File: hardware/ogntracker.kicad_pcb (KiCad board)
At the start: 2 copper layers, 50 x 84 mm, 29 parts, among them J1 ANT, J2 LX, J3 IGC, U1 STM32DEVBOARD, U2 RFM69HW, U3 VK2828U7G5LF, U4 MAX232

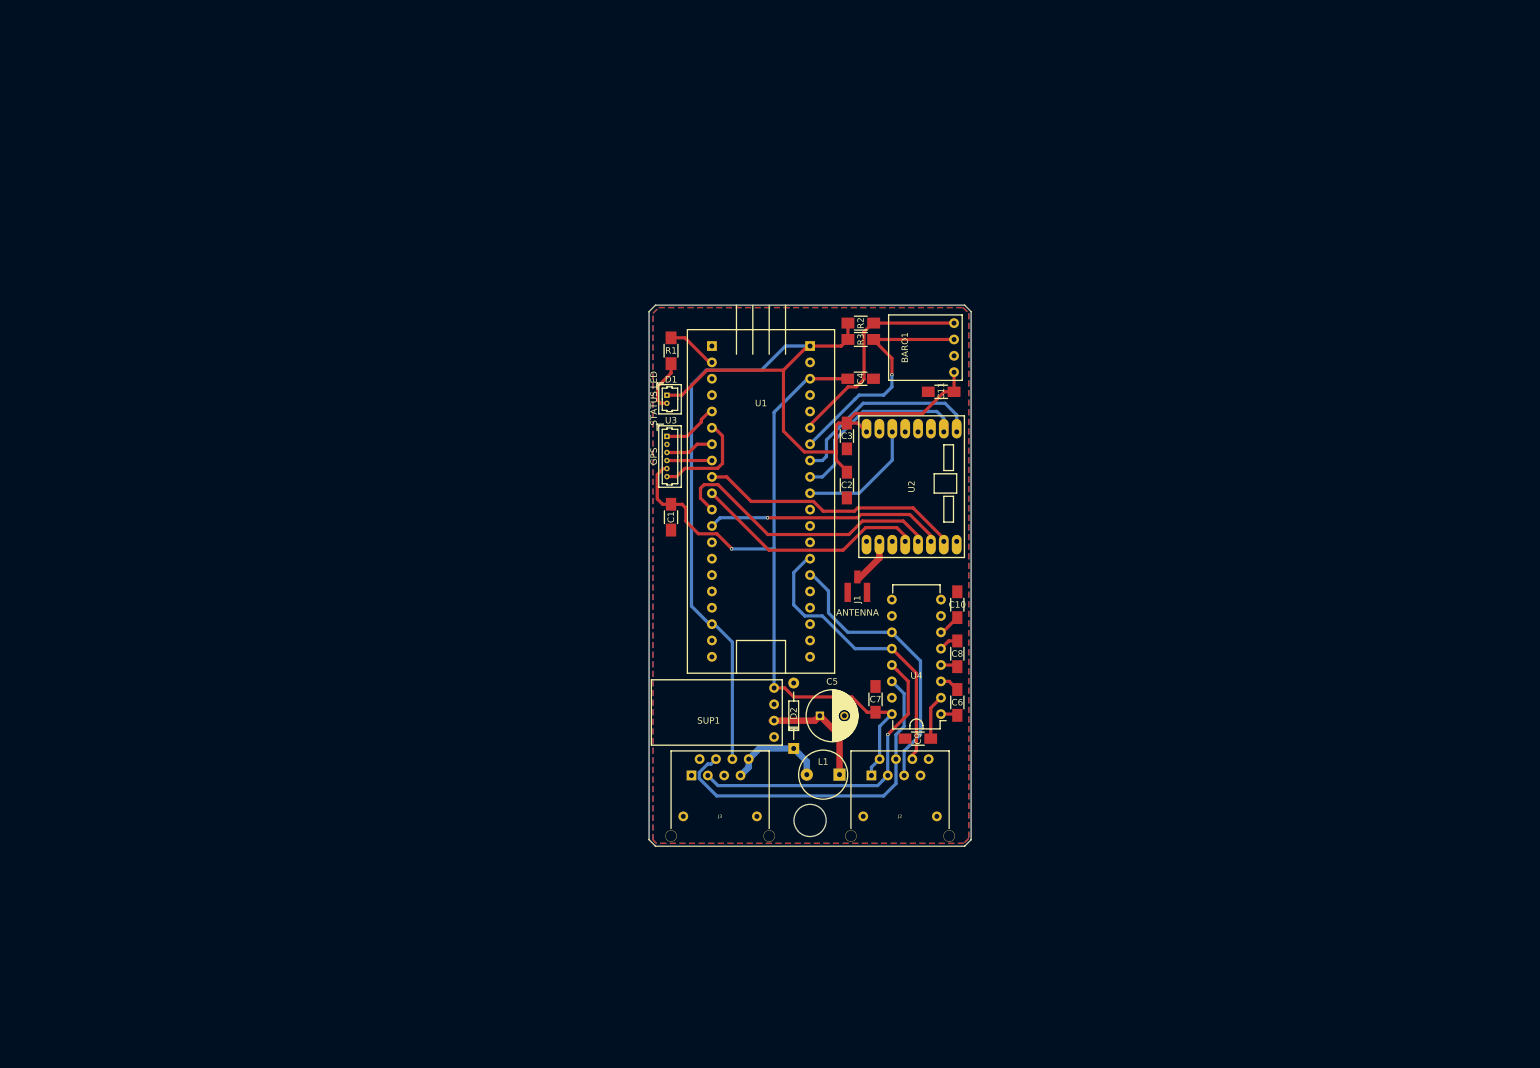
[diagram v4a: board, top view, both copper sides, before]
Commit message: Various updates to schematics and experiments with layout for new box
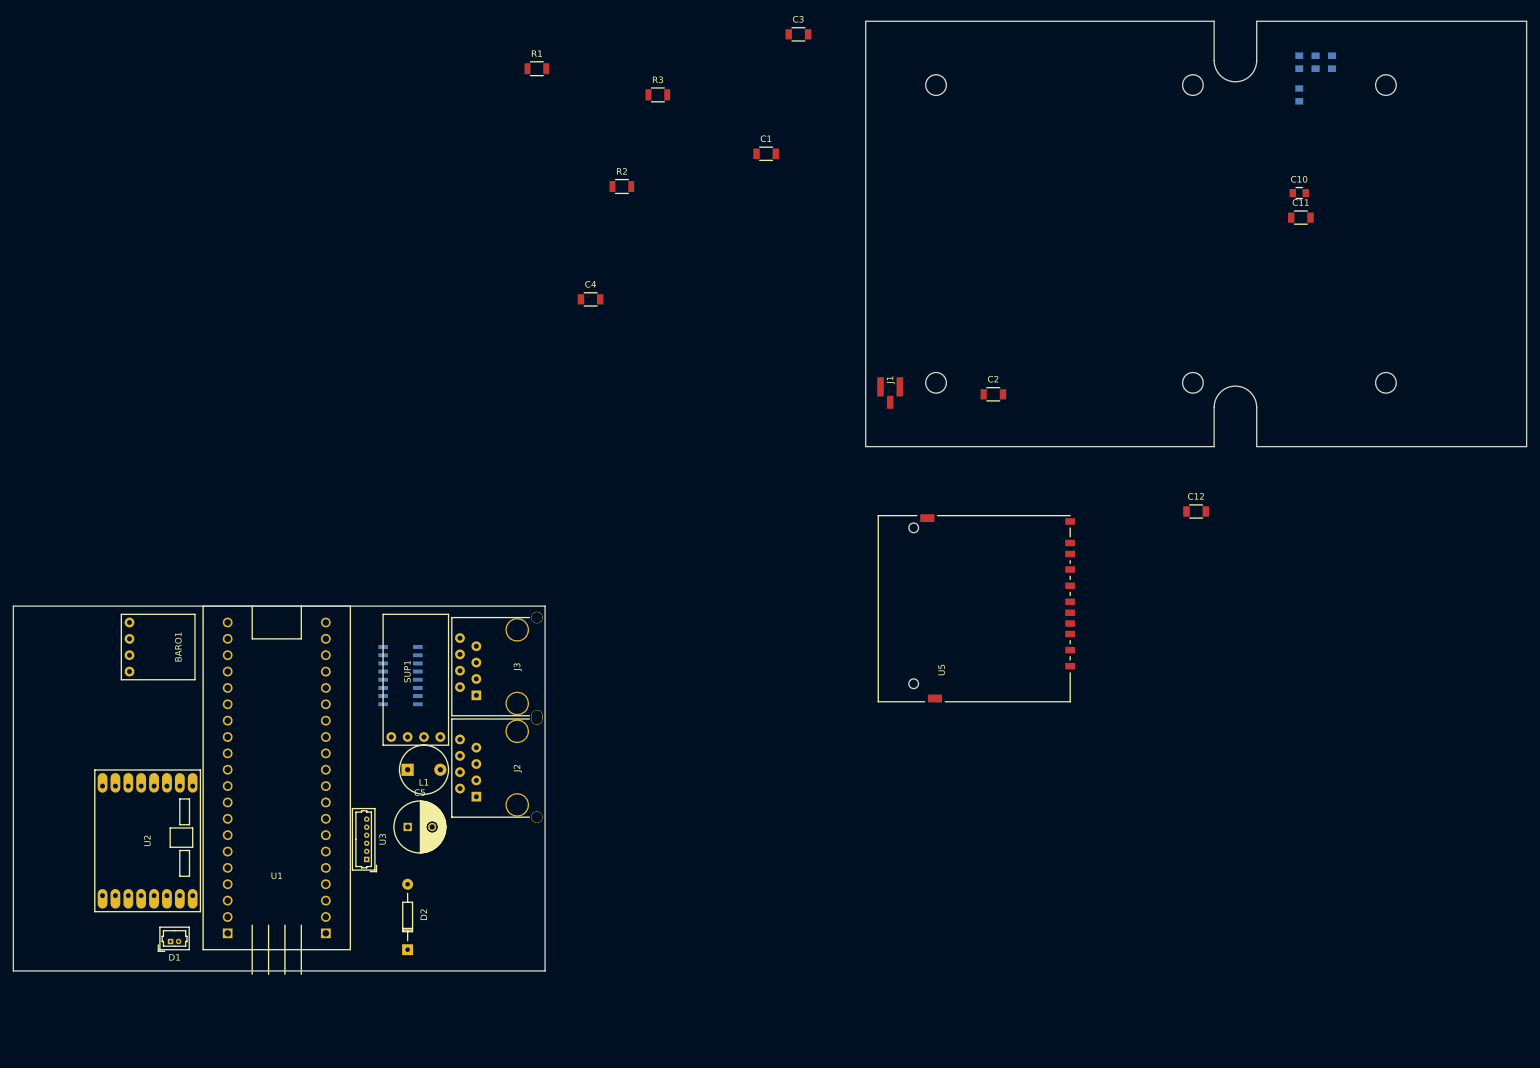
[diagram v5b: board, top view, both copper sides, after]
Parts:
- removed the REF** at (155.7, 152.7)
- removed REF***: OSHW-Logo2_7.3x6mm_SilkScreen, Symbols:OSHW-Logo2_7.3x6mm_SilkScreen
- removed REF***: KiCad-Logo2_6mm_SilkScreen, Symbols:KiCad-Logo2_6mm_SilkScreen
- added C12: 100nF, Capacitors_SMD:C_1206, F.Cu at (215.6, 104.7)
- added REF**: MountingHole_3.2mm_M3, Mounting_Holes:MountingHole_3.2mm_M3, F.Cu at (175.2, 84.8)
- added REF**: MountingHole_3.2mm_M3, Mounting_Holes:MountingHole_3.2mm_M3, F.Cu at (175.2, 38.5)
- added REF**: MountingHole_3.2mm_M3, Mounting_Holes:MountingHole_3.2mm_M3, F.Cu at (215.1, 84.8)
- added REF**: MountingHole_3.2mm_M3, Mounting_Holes:MountingHole_3.2mm_M3, F.Cu at (215.1, 38.5)
- added REF**: MountingHole_3.2mm_M3, Mounting_Holes:MountingHole_3.2mm_M3, F.Cu at (245.1, 38.5)
- added REF**: MountingHole_3.2mm_M3, Mounting_Holes:MountingHole_3.2mm_M3, F.Cu at (245.1, 84.8)
- added U5: SDCARD_SPI, Connect:SD_Card_Receptacle, F.Cu at (196.1, 119.4)
- C1, C11, C2, C3, C4: footprint Capacitors_SMD:C_1206_HandSoldering -> Capacitors_SMD:C_1206
- C10: footprint Capacitors_SMD:C_1206_HandSoldering -> Capacitors_SMD:C_0805
- C6, C7, C8, C9: footprint Capacitors_SMD:C_1206_HandSoldering -> Capacitors_SMD:C_0805; moved to B.Cu
- R1: value 330 -> 90; footprint Resistors_SMD:R_1206_HandSoldering -> Resistors_SMD:R_1206
- R2, R3: footprint Resistors_SMD:R_1206_HandSoldering -> Resistors_SMD:R_1206
- U4: footprint OGN Tracker:DIP-16_W7.62mm -> Housings_SOIC:SOIC-16_3.9x9.9mm_Pitch1.27mm; moved to B.Cu
- moved BARO1 131.4 mm to (52.6, 125.8), turned to 270 degrees
- moved U2 130.7 mm to (52.8, 155.9)
- moved C9 121.8 mm to (234.2, 35.0), turned to 270 degrees
- moved C7 121.7 mm to (236.7, 35.0)
- moved D1 114.6 mm to (56.4, 171.5), turned to 0 degrees
- moved C6 112.7 mm to (231.6, 35.0), turned to 270 degrees
- moved C8 101.7 mm to (231.6, 40.1), turned to 270 degrees
- moved U1 87.9 mm to (72.9, 147.4), turned to 180 degrees
- moved U4 84.1 mm to (92.1, 130.2), turned to 0 degrees
- moved C10 83.1 mm to (231.6, 55.3), turned to 0 degrees
- moved U3 80.5 mm to (86.9, 158.8), turned to 90 degrees
- moved D2 67.6 mm to (93.2, 172.8)
- moved C5 66.3 mm to (93.2, 153.7)
- moved C3 62.8 mm to (153.9, 30.7), turned to 0 degrees
- moved C11 62.1 mm to (231.9, 59.1), turned to 0 degrees
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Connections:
- U1 pad 37: (no net) -> /SD_MOSI
- U1 pad 38: (no net) -> /SD_MISO
- U1 pad 39: (no net) -> /SD_SCK
- U1 pad 40: (no net) -> /SD_CS
- U3 pad 1: /GPS_ENABLE -> /GPS_PPS
- U3 pad 2: Earth -> 5V
- U3 pad 3: /GPS_TXD -> /GPS_RXD
- U3 pad 4: /GPS_RXD -> /GPS_TXD
- U3 pad 5: 5V -> Earth
- U3 pad 6: /GPS_PPS -> /GPS_ENABLE
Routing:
- net 3.3V: track 170.5 -> 0.00 mm
- net 5V: track 115.4 -> 0.00 mm, vias 1 -> 0
- net /RS232_TX: track 54.0 -> 0.00 mm
- net /RS232_RX: track 48.8 -> 0.00 mm, vias 1 -> 0
- net /CON1_RXD: track 45.9 -> 0.00 mm
- net /SPI_MISO: track 44.4 -> 0.00 mm
- net /CON1_TXD: track 43.5 -> 0.00 mm
- net /SPI_SELECT: track 40.8 -> 0.00 mm
- net /SPI_MOSI: track 39.2 -> 0.00 mm, vias 1 -> 0
- net /BARO_SCL: track 37.8 -> 0.00 mm, vias 1 -> 0
- net /SPI_CLOCK: track 37.6 -> 0.00 mm
- net /BARO_SDA: track 33.7 -> 0.00 mm
- net /CHIP_RESET: track 32.1 -> 0.00 mm
- net /INT_REQ: track 30.1 -> 0.00 mm
- net /AUX_STATUS: track 19.3 -> 0.00 mm
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- removed copper zone on B.Cu, net Earth
- removed copper zone on F.Cu, net Earth
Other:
- board size 50 x 84 mm -> 235 x 147.4 mm
- board text removed: "ANTENNA"
- board text removed: "Based on design by http://glidernet.org. See https://github.com/kedder/kedtracker for more info."
- board text removed: "GPS"
- board text removed: "IGC"
- board text removed: "Ked Tracker v0.3"
- board text removed: "LX"
- board text removed: "STATUS LED"

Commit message: Routed prototype board for HAMMOND 1593N box
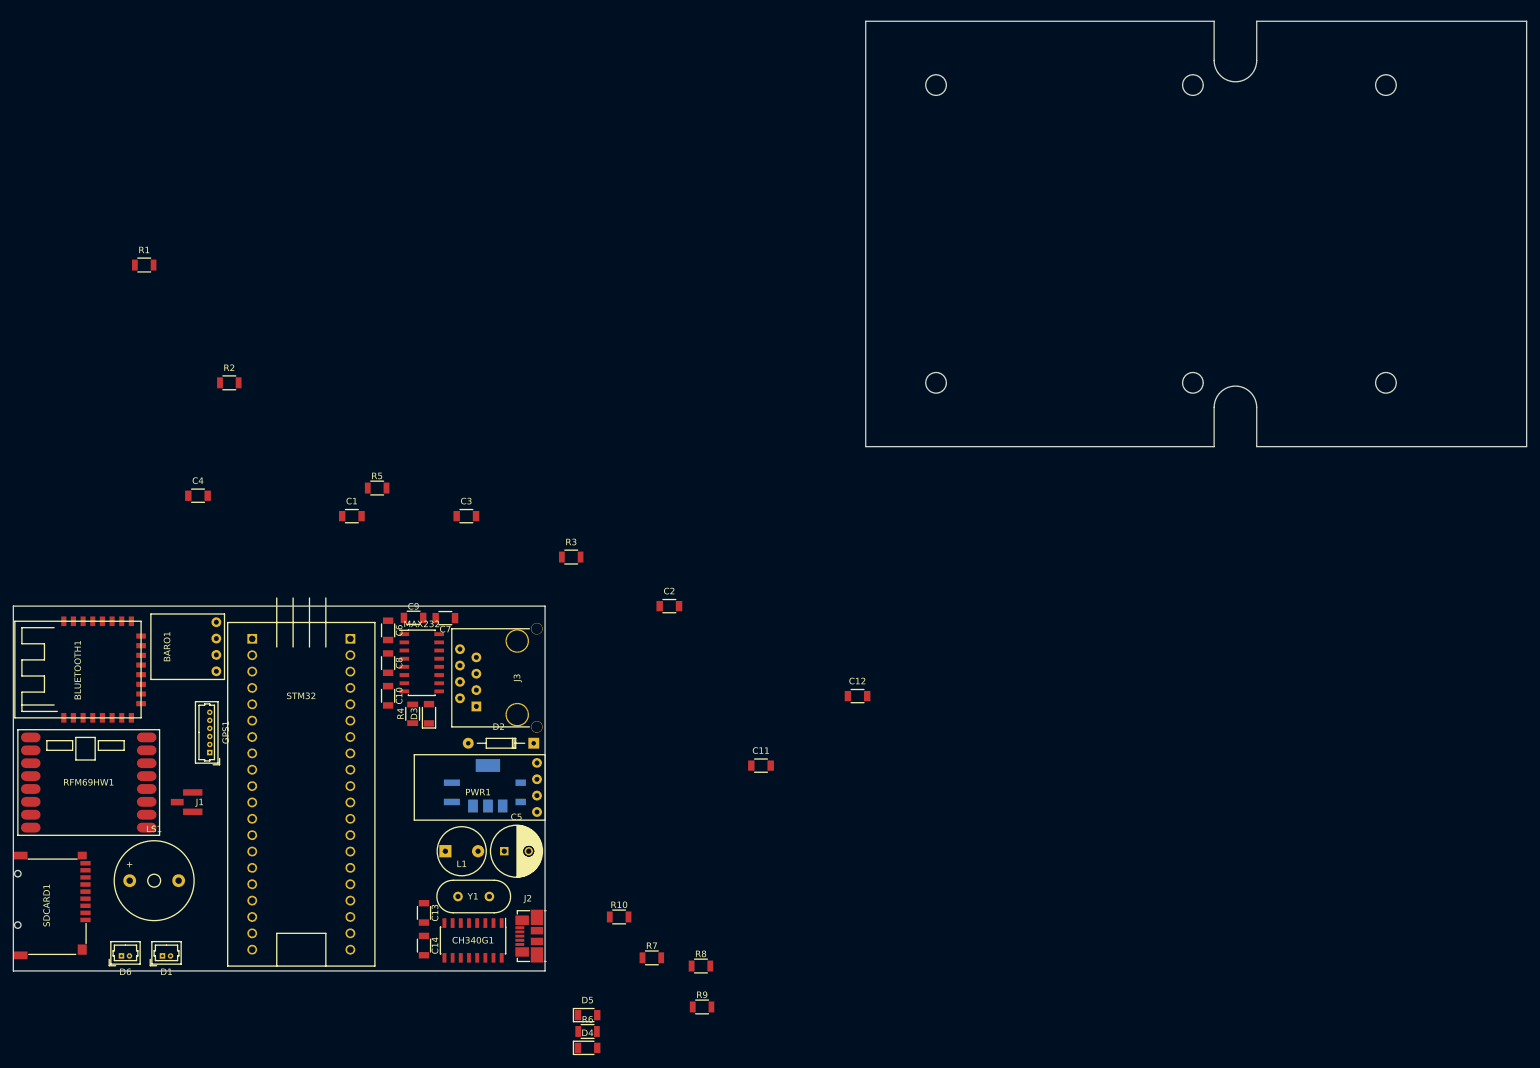
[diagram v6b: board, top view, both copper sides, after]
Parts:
- removed SUP1: BUCK_CVTR, OGN Tracker:Buck_Converter_Sm
- removed U2: RFM69HW, OGN Tracker:RFM69HW
- removed U3: VK2828U7G5LF, OGN Tracker:Molex_PicoBlade_53047-0610_06x1.25mm_Straight
- removed U4: MAX232, Housings_SOIC:SOIC-16_3.9x9.9mm_Pitch1.27mm
- removed U5: SDCARD_SPI, Connect:SD_Card_Receptacle
- added BLUETOOTH1: JDY-08, OGN Tracker:JDY-08, F.Cu at (51.8, 136.8)
- added C13: 22pF, Capacitors_SMD:C_1206, F.Cu at (95.7, 167.1)
- added C14: 22pF, Capacitors_SMD:C_1206, F.Cu at (95.7, 172.1)
- added C15: 47uF, Capacitors_SMD:C_1210, B.Cu at (100.1, 148.3)
- added C16: 1uF, Capacitors_SMD:C_1206, B.Cu at (110.7, 148.3)
- added CH340G1: CH340G, Housings_SOIC:SOIC-16_3.9x9.9mm_Pitch1.27mm, F.Cu at (103.4, 171.3)
- added D3: 1N4148, Diodes_SMD:D_1206, F.Cu at (96.5, 136.1)
- added D4: 1N4148, Diodes_SMD:D_1206, F.Cu at (121.1, 188.0)
- added D5: 1N4148, Diodes_SMD:D_1206, F.Cu at (121.1, 182.9)
- added D6: LED_BT, OGN Tracker:Molex_PicoBlade_53047-0210_02x1.25mm_Straight, F.Cu at (48.8, 173.7)
- added GPS1: VK2828U7G5LF, OGN Tracker:Molex_PicoBlade_53047-0610_06x1.25mm_Straight, F.Cu at (62.5, 142.2)
- added LS1: Buzzer, Buzzers_Beepers:Buzzer_12x9.5RM7.6, F.Cu at (53.8, 162.1)
- added MAX232: MAX232, Housings_SOIC:SOIC-16_3.9x9.9mm_Pitch1.27mm, F.Cu at (95.4, 128.2)
- added PWR1: BUCK_CVTR, OGN Tracker:Buck_Converter_Sm, F.Cu at (108.2, 147.6)
- added R10: 82, Resistors_SMD:R_1206, F.Cu at (126.0, 167.7)
- added R4: 10K, Resistors_SMD:R_1206, F.Cu at (94.0, 136.1)
- added R5: 10K, Resistors_SMD:R_1206, F.Cu at (88.5, 101.1)
- added R6: 10K, Resistors_SMD:R_1206, F.Cu at (121.1, 185.5)
- added R7: 10K, Resistors_SMD:R_1206, F.Cu at (131.1, 174.0)
- added R8: 10K, Resistors_SMD:R_1206, F.Cu at (138.7, 175.3)
- added R9: 10K, Resistors_SMD:R_1206, F.Cu at (138.9, 181.7)
- added RFM69HW1: RFM69HW, OGN Tracker:RFM69HW, F.Cu at (43.7, 146.8)
- added SDCARD1: Micro SD Reader, OGN Tracker:SDCARD_BOMB, F.Cu at (32.7, 165.9)
- added STM32: STM32DEVBOARD, OGN Tracker:STM32DEVBOARD, F.Cu at (76.7, 147.4)
- added Y1: 12M, Crystals:Crystal_HC49-4H_Vertical, F.Cu at (105.9, 164.5)
- C10: value 1uF -> 100nF; footprint Capacitors_SMD:C_0805 -> Capacitors_SMD:C_1206
- C6, C7, C8, C9: value 1uF -> 100nF; footprint Capacitors_SMD:C_0805 -> Capacitors_SMD:C_1206; moved to F.Cu
- D1: value LED -> LED_STAT
- J2: value LX -> Micro USB; footprint OGN Tracker:RJ45_SOCKET_SHLD -> Connectors_Molex:USB_Micro-B_Molex_47346-0001
- R1: value 90 -> 82
- U1: value STM32DEVBOARD -> LM2936-3.3; footprint OGN Tracker:STM32DEVBOARD -> TO_SOT_Packages_SMD:SOT-223-3Lead_TabPin2; moved to B.Cu
- moved C6 166.7 mm to (90.2, 123.2)
- moved C8 166.7 mm to (90.2, 128.3)
- moved C9 164.5 mm to (94.1, 121.2), turned to 0 degrees
- moved C7 162.5 mm to (99.1, 121.3), turned to 180 degrees
- moved C10 161.6 mm to (90.2, 133.3), turned to 270 degrees
- moved J1 126.2 mm to (59.4, 149.9), turned to 180 degrees
- moved C11 119.4 mm to (148.1, 144.2)
- moved C3 90.8 mm to (102.3, 105.5)
- moved C1 85.5 mm to (84.5, 105.5)
- moved R3 73.0 mm to (118.6, 111.8)
- moved C4 68.2 mm to (60.7, 102.3)
- moved R1 68.2 mm to (52.3, 66.5)
- moved R2 68.2 mm to (65.5, 84.8)
- moved C2 60.1 mm to (133.8, 119.4)
- moved C12 59.9 mm to (163.1, 133.4)
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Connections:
- C12 pad 1: Earth -> 3.3V
- C12 pad 2: 3.3V -> Earth
- C4 pad 2: 5V -> 3.3V
- C7 pad 2: 5V -> 3.3V
- J2 pad 2: 5V -> Net-(CH340G1-Pad6)
- J2 pad 3: /RS232_RX -> Net-(CH340G1-Pad5)
- J2 pad 4: /RS232_TX -> (no net)
- J2 pad 5: /CON1_TXD -> Earth
- J2 pad 6: /CON1_RXD -> Earth
- J3 pad 3: /RS232_RX -> Net-(J3-Pad3)
- J3 pad 4: /RS232_TX -> Net-(J3-Pad4)
- U1 pad 1: (no net) -> 5V
- U1 pad 2: /LED -> Earth
- U1 pad 3: (no net) -> 3.3V

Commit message: Unfinished pcb layouts
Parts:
- removed the REF** at (175.2, 84.8)
- removed the REF** at (175.2, 38.5)
- removed the REF** at (215.1, 84.8)
- removed the REF** at (215.1, 38.5)
- removed the REF** at (245.1, 38.5)
- removed the REF** at (245.1, 84.8)
- added C17: 100nF, Capacitors_SMD:C_1206, F.Cu at (106.4, 80.0)
- added C18: 100nF, Capacitors_SMD:C_1206, B.Cu at (166.7, 96.8)
- added F1: 0.5A, Fuse_Holders_and_Fuses:Fuse_SMD1206_Reflow, B.Cu at (167.3, 67.0)
- added F2: 0.5A, Fuse_Holders_and_Fuses:Fuse_SMD1206_Reflow, B.Cu at (174.9, 54.3)
- added REF**: MountingHole_3.2mm_M3, Mounting_Holes:MountingHole_3.2mm_M3, F.Cu at (114.3, 57.7)
- added REF**: MountingHole_3.2mm_M3, Mounting_Holes:MountingHole_3.2mm_M3, F.Cu at (168.3, 85.7)
- BARO1: footprint OGN Tracker:BMP280 -> OGN Tracker:BMP280_HandSoldering
- C1, C10, C11, C2, C3, C4, C6, C7, C8, C9, CH340G1, D3, D4, D5, R1, R10, R2, R3, R4, R5, R6, R7, R8, R9, RFM69HW1: moved to B.Cu
- C13, C14: footprint Capacitors_SMD:C_1206 -> Capacitors_SMD:C_0603_HandSoldering; moved to B.Cu
- C15, C16, U1: moved to F.Cu
- C5: footprint Capacitors_ThroughHole:C_Radial_D8_L13_P3.8 -> Capacitors_ThroughHole:CP_Radial_D8.0mm_P3.80mm
- D1, D6: footprint OGN Tracker:Molex_PicoBlade_53047-0210_02x1.25mm_Straight -> OGN Tracker:Molex_PicoBlade_02x1.25mm_HandSoldering
- D2: footprint Diodes_ThroughHole:Diode_DO-35_SOD27_Horizontal_RM10 -> Diodes_SMD:D_SMA_Standard; moved to B.Cu
- GPS1: footprint OGN Tracker:Molex_PicoBlade_53047-0610_06x1.25mm_Straight -> Pin_Headers:Pin_Header_Straight_1x06_Pitch2.00mm
- MAX232: value MAX232 -> MAX3232; moved to B.Cu
- PWR1: footprint OGN Tracker:Buck_Converter_Sm -> OGN Tracker:Buck_Converter_Sm_HandSoldering
- STM32: footprint OGN Tracker:STM32DEVBOARD -> OGN Tracker:STM32DEVBOARD_HandSoldering
- moved D6 148.6 mm to (162.2, 77.8), turned to 180 degrees
- moved D1 147.7 mm to (162.2, 72.1), turned to 180 degrees
- moved L1 133.6 mm to (178.1, 47.9)
- moved C5 126.6 mm to (171.8, 47.9), turned to 180 degrees
- moved LS1 123.9 mm to (106.4, 49.8)
- moved PWR1 111.2 mm to (174.3, 58.1)
- moved D4 111.2 mm to (148.5, 80.2)
- moved GPS1 110.8 mm to (133.8, 57.5), turned to 270 degrees
- moved C14 110.6 mm to (163.5, 84.8), turned to 90 degrees
- moved C4 110.0 mm to (157.7, 50.5), turned to 90 degrees
- moved U1 108.3 mm to (162.2, 54.9)
- moved C15 107.4 mm to (164.5, 62.4), turned to 270 degrees
- moved RFM69HW1 106.7 mm to (126.0, 78.9), turned to 270 degrees
- moved R1 106.2 mm to (158.4, 71.4), turned to 270 degrees
- moved C10 105.4 mm to (149.1, 46.0), turned to 0 degrees
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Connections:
- net Net-(C13-Pad2) renamed /Console/USB_XI
- net Net-(C14-Pad2) renamed /Console/USB_XO
- net Net-(CH340G1-Pad2) renamed /Console/USB_TX
- net Net-(CH340G1-Pad5) renamed /Console/USB_D+
- net Net-(CH340G1-Pad6) renamed /Console/USB_D-
- net Net-(D3-Pad1) renamed /Console/MAX232_TX
- net Net-(J3-Pad3) renamed /Console/RS232_RX
- net Net-(J3-Pad4) renamed /Console/RS232_TX
- BARO1 pad 1: 3.3V -> /BARO_SDA
- BARO1 pad 2: Earth -> /BARO_SCL
- BARO1 pad 3: /BARO_SCL -> Earth
- BARO1 pad 4: /BARO_SDA -> 3.3V
- BLUETOOTH1 pad 19: /CON1_TXD -> /Console/BT_TX
- BLUETOOTH1 pad 20: Net-(BLUETOOTH1-Pad20) -> /CON1_TXD
- C1 pad 1: 5V -> /5V_PROT
- C16 pad 1: 5V -> /5V_PROT
- C9 pad 1: Earth -> 3.3V
- D2 pad 1: +12V -> /SUP_PROT
- D4 pad 1: Net-(BLUETOOTH1-Pad20) -> /Console/BT_TX
- GPS1 pad 2: 5V -> /5V_PROT
- L1 pad 2: +12V -> /SUP_PROT
- R5 pad 1: Net-(BLUETOOTH1-Pad20) -> /Console/BT_TX
- U1 pad 1: 5V -> /5V_PROT
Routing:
- net 3.3V: track 0.00 -> 232.5 mm, vias 0 -> 7
- net 5V: track 0.00 -> 53.0 mm, vias 0 -> 3
- net /5V_PROT: track 0.00 -> 52.6 mm, vias 0 -> 2
- net /SUP_PROT: track 0.00 -> 26.8 mm, vias 0 -> 2
- net /SUP_CLEAN: track 0.00 -> 26.4 mm, vias 0 -> 2
- net Earth: track 0.00 -> 9.49 mm
- net +12V: track 0.00 -> 5.92 mm
- added copper zone on B.Cu, net Earth
- added copper zone on F.Cu, net Earth
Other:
- board size 235 x 147.4 mm -> 82.7 x 56.6 mm
- net class ANT: trace_width 1 -> 3.23; via_dia 0.5 -> 1.5; via_drill 0.3 -> 0.5
- net class Default: trace_width 0.5 -> 0.3; via_dia 0.5 -> 1.5; via_drill 0.3 -> 0.5
- net class HV: via_dia 0.5 -> 1.8; via_drill 0.3 -> 0.5
- net class PWR: via_dia 0.5 -> 1.5; via_drill 0.3 -> 0.5
- rule trace_min: 0.2 -> 0
- board text added: "Front"
- board text added: "Hammond 1593L"
- board text added: "Rear"
